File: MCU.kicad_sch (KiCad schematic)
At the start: 16 parts, among them SW1 SW_SPDT, U1 STM32F091RCTx, Y1 16MHz

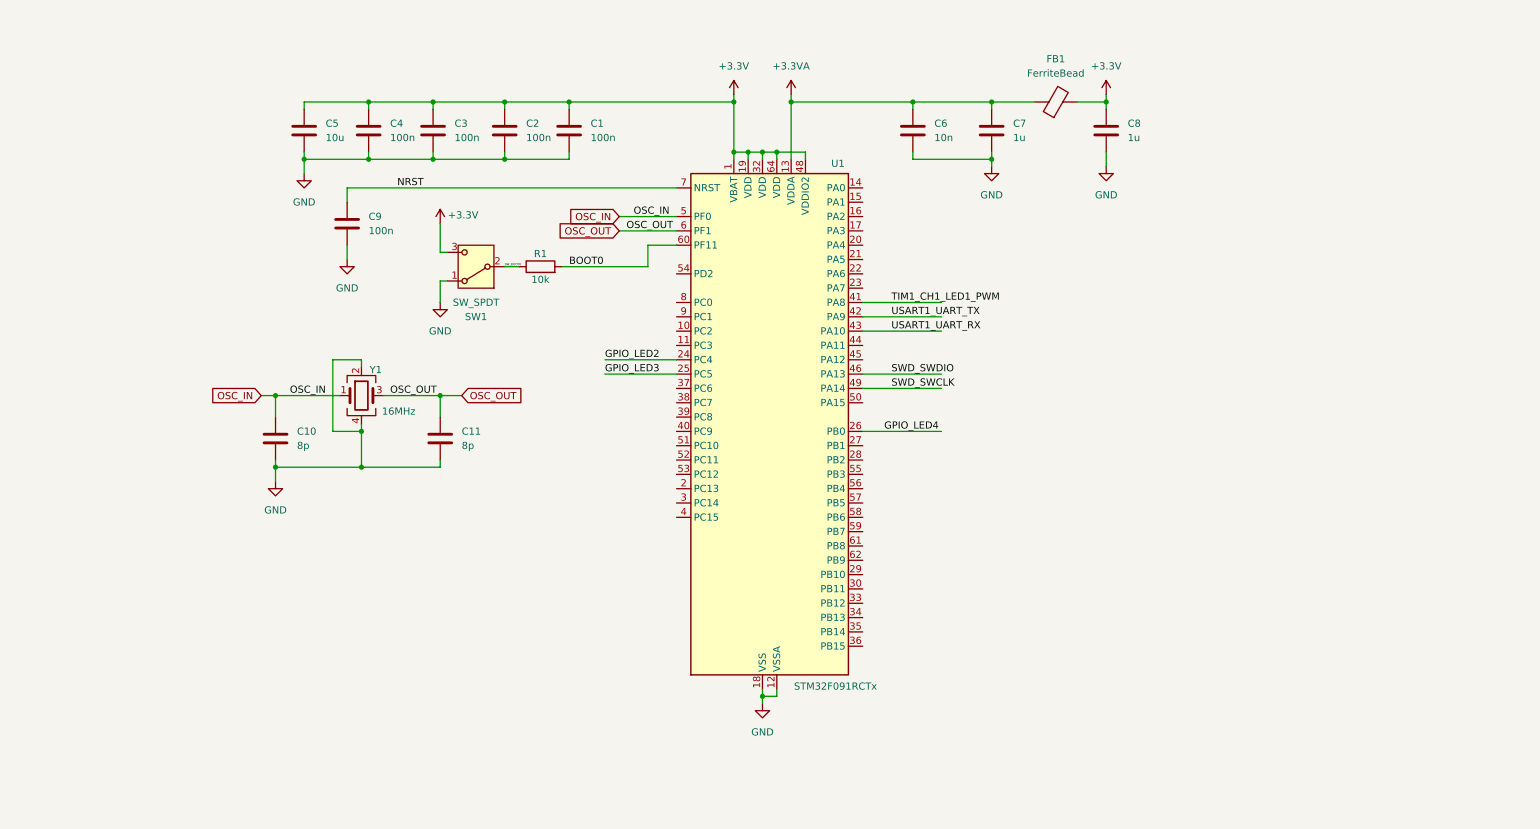
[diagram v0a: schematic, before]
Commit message: Finished Schematic design, moving on to PCB layout and routing
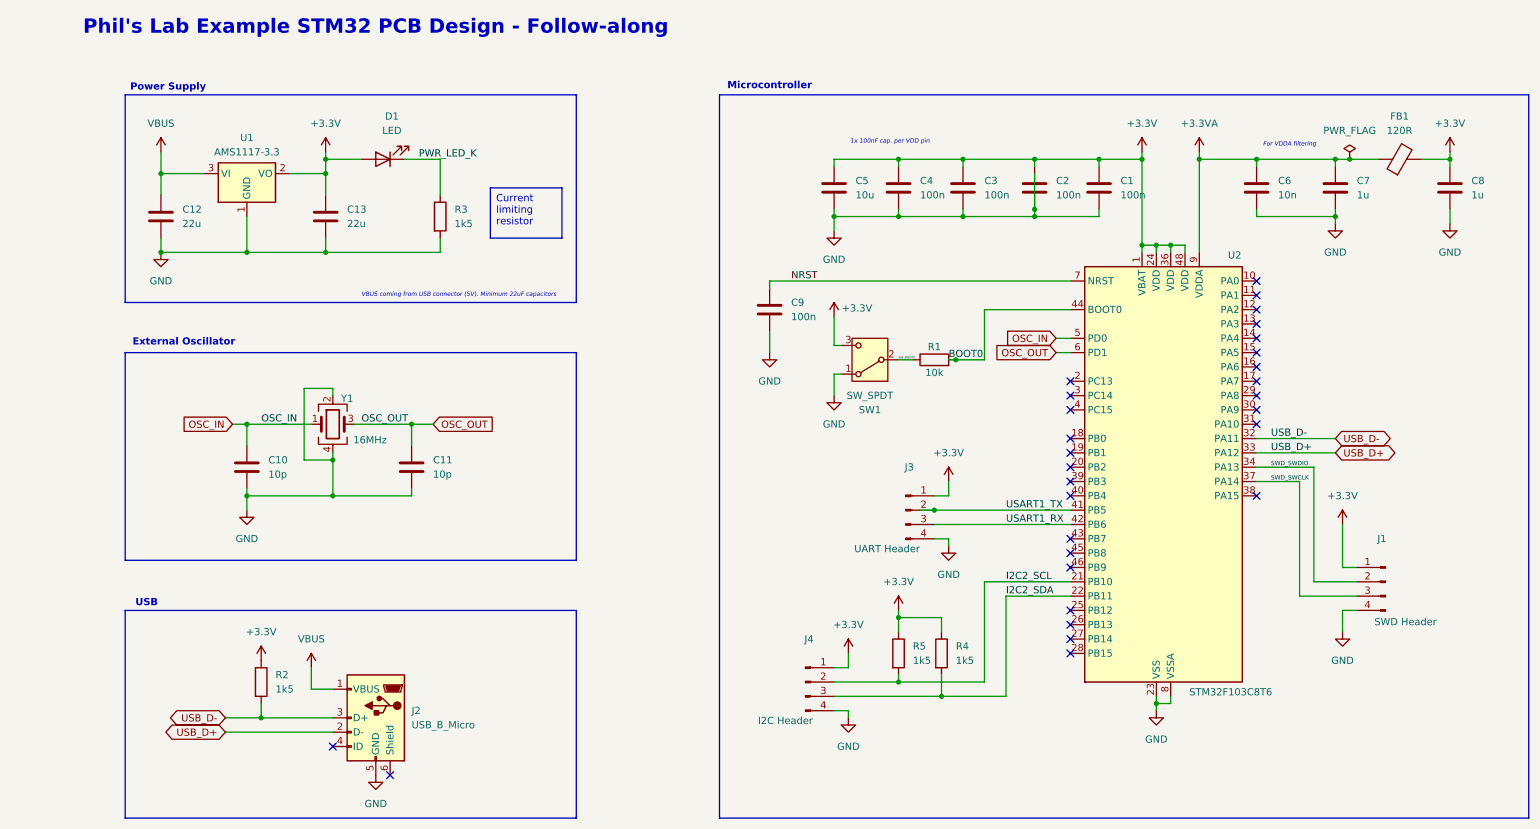
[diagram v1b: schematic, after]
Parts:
- removed U1: STM32F091RCTx, Package_QFP:LQFP-64_10x10mm_P0.5mm, symbol MCU_ST_STM32F0:STM32F091RCTx
- added C12, C13: 22u, Capacitor_SMD:C_0805_2012Metric, symbol Device:C
- added D1: LED, LED_SMD:LED_0603_1608Metric, symbol Device:LED
- added J1: SWD Header, Connector_PinHeader_2.54mm:PinHeader_1x04_P2.54mm_Vertical, symbol Connector:Conn_01x04_Pin
- added J2: USB_B_Micro, Connector_USB:USB_Micro-B_Wuerth_629105150521, symbol Connector:USB_B_Micro
- added J3: UART Header, Connector_PinHeader_2.54mm:PinHeader_1x04_P2.54mm_Vertical, symbol Connector:Conn_01x04_Pin
- added J4: I2C Header, Connector_PinHeader_2.54mm:PinHeader_1x04_P2.54mm_Vertical, symbol Connector:Conn_01x04_Pin
- added R2, R3, R4, R5: 1k5, Resistor_SMD:R_0402_1005Metric, symbol Device:R
- added U1: AMS1117-3.3, Package_TO_SOT_SMD:SOT-223-3_TabPin2, symbol Regulator_Linear:AMS1117-3.3
- added U2: STM32F103C8T6, Package_QFP:LQFP-48_7x7mm_P0.5mm, symbol MCU_ST_STM32F1:STM32F103C8Tx
- C1, C2, C3, C4, C7, C8, C9: footprint (none) -> Capacitor_SMD:C_0402_1005Metric
- C10, C11: value 8p -> 10p; footprint (none) -> Capacitor_SMD:C_0402_1005Metric
- C5, C6: footprint (none) -> Capacitor_SMD:C_0603_1608Metric
- FB1: value FerriteBead -> 120R; footprint (none) -> Inductor_SMD:L_0603_1608Metric
- R1: footprint (none) -> Resistor_SMD:R_0402_1005Metric
- SW1: footprint (none) -> Button_Switch_THT:SW_E-Switch_EG1224_SPDT_Angled
- Y1: footprint (none) -> Crystal:Crystal_SMD_3225-4Pin_3.2x2.5mm
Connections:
- net +3.3V: now also C13.1, D1.2 (A), J1.1 (Pin_1), J3.1 (Pin_1), J4.1 (Pin_1), R2.1, R4.1, R5.1, U1.2 (VO), U2.1 (VBAT), U2.24 (VDD), U2.36 (VDD), U2.48 (VDD)
- net +3.3VA: now also U2.9 (VDDA)
- net BOOT0: now also U2.44 (BOOT0)
- net GND: now also C12.2, C13.2, J1.4 (Pin_4), J2.5 (GND), J3.4 (Pin_4), J4.4 (Pin_4), R3.2, U1.1 (GND), U2.23 (VSS), U2.35 (VSS), U2.47 (VSS), U2.8 (VSSA)
- net NRST: now also U2.7 (NRST)
- net OSC_IN: now also U2.5 (PD0)
- net OSC_OUT: now also U2.6 (PD1)
- net SWD_SWCLK: now also J1.3 (Pin_3), U2.37 (PA14)
- net SWD_SWDIO: now also J1.2 (Pin_2), U2.34 (PA13)
- new net I2C2_SCL: J4.2 (Pin_2), R5.2, U2.21 (PB10)
- new net I2C2_SDA: J4.3 (Pin_3), R4.2, U2.22 (PB11)
- new net PWR_LED_K: D1.1 (K), R3.1
- new net USART1_RX: J3.3 (Pin_3), U2.42 (PB6)
- new net USART1_TX: J3.2 (Pin_2), U2.41 (PB5)
- new net USB_D+: J2.2 (D-), U2.33 (PA12)
- new net USB_D-: J2.3 (D+), R2.2, U2.32 (PA11)
- new net VBUS: C12.1, J2.1 (VBUS), U1.3 (VI)
- no-connect marks 0 -> 29
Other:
- note added: "1x 100nF cap. per VDD pin"
- note added: "External Oscillator"
- note added: "For VDDA filtering"
- note added: "Microcontroller"
- note added: "Phil's Lab Example STM32 PCB Design - Follow-along"
- note added: "Power Supply"
- note added: "USB"
- note added: "VBUS coming from USB connector (5V). Minimum 22uF capacitors"
- company: (none) -> Tudor Donca
- title: (none) -> Phil's Lab Example STM32 PCB Design - Follow-along
- moved on the sheet: C1, C10, C11, C2, C3, C4, C5, C6, C7, C8, C9, FB1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
